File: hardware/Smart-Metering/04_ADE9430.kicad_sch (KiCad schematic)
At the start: 14 parts, among them U401 ADE9430ACPZ, Y401 24.576MHz

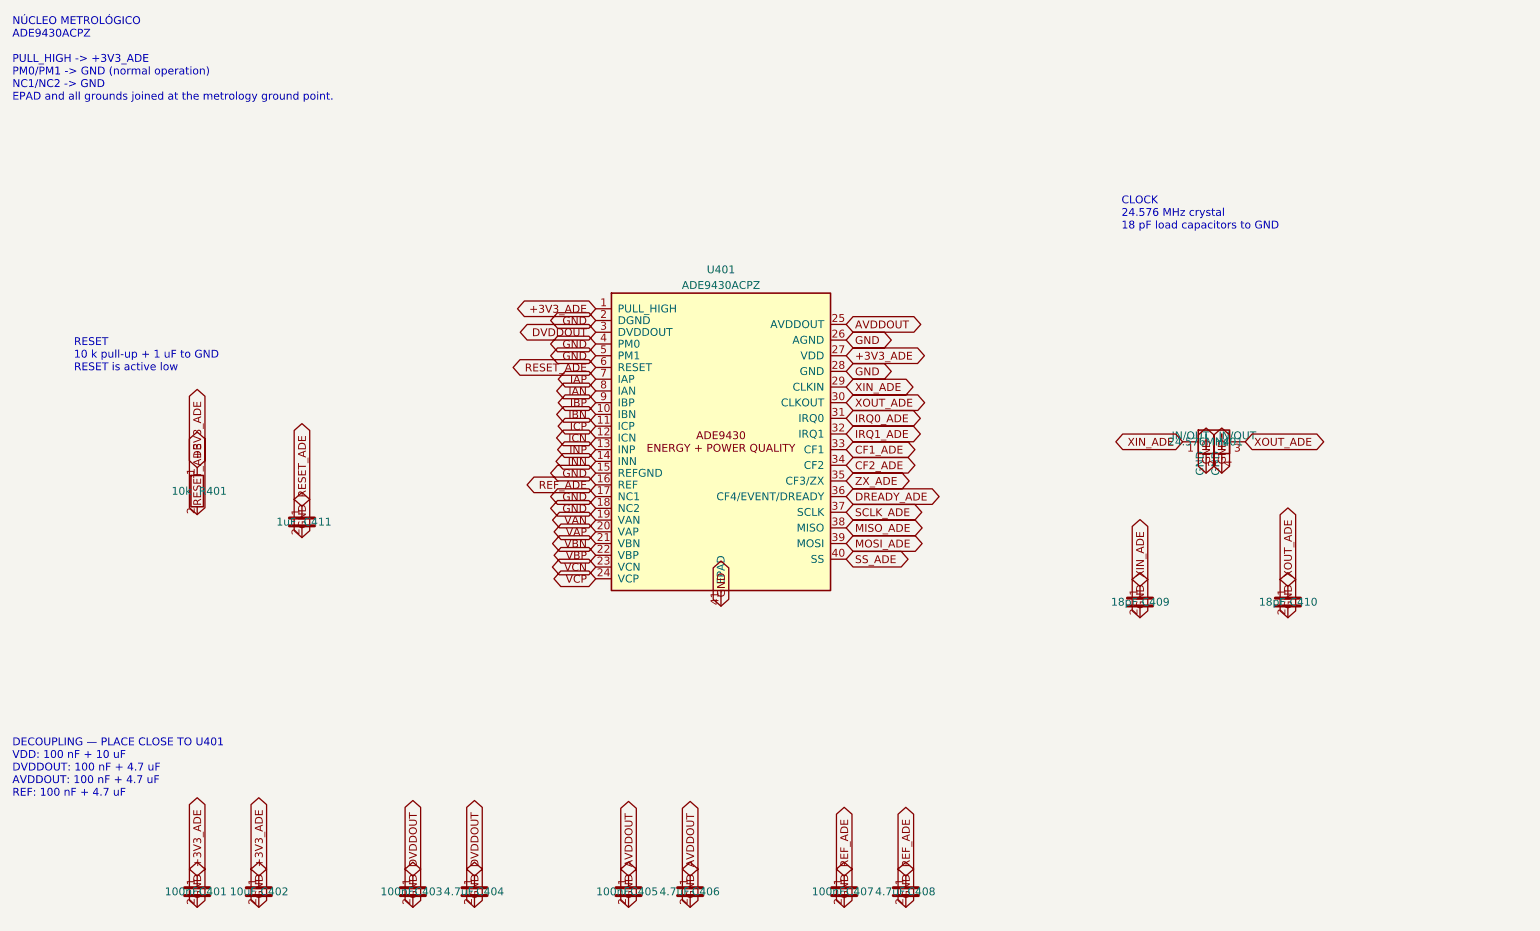
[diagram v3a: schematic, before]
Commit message: Resolve as pendências da revisão do esquemático
P1  ADE9430: footprint VQFN-40 6x6 com EP de 4,15 mm, compatível com as
    variantes CP-40 de 6x6 mm (EP de 3,9 a 4,7 mm).
P2  Confirmado no datasheet: MISO solto com SS alto (pull-up de 100 kΩ)
    e NC1/NC2 em GND, como já estava.
P3  J301-J304: headers JST PH de 4 vias cabeados até conectores M8
    fêmea de painel (à prova de toque).
P4  PS601 -> U606 ADuM6000 (isoPower 5 kVrms, símbolo oficial).
P5  PS101 -> RAC20-05SK/277 (85-305 VAC, 120-430 VDC, 20 W); fusíveis
    T500mA, R101 3 W, C101 10 uF/450 V; entrada do BQ25895 a 3 A.
P7  TPS61089 -> TPS61022 (compensação interna, sem valores a ajustar).
P8  Placa EV alimentada pelos pinos 5 V do J1 (nota na folha 07).
P9  EEPROM de calibração 24LC64 no I2C1.
P10 Labels globais de uma só folha convertidos em locais.

Verificação: 223 componentes, nenhum pino solto, nenhuma net sem fonte,
nenhum conflito de saída, isolação íntegra, todos os footprints
existentes na biblioteca oficial do KiCad.

Co-Authored-By: Claude Opus 5.5 <noreply@anthropic.com>
Claude-Session: https://claude.ai/code/session_012B8cVkhtjf3eg98UdpNCpf
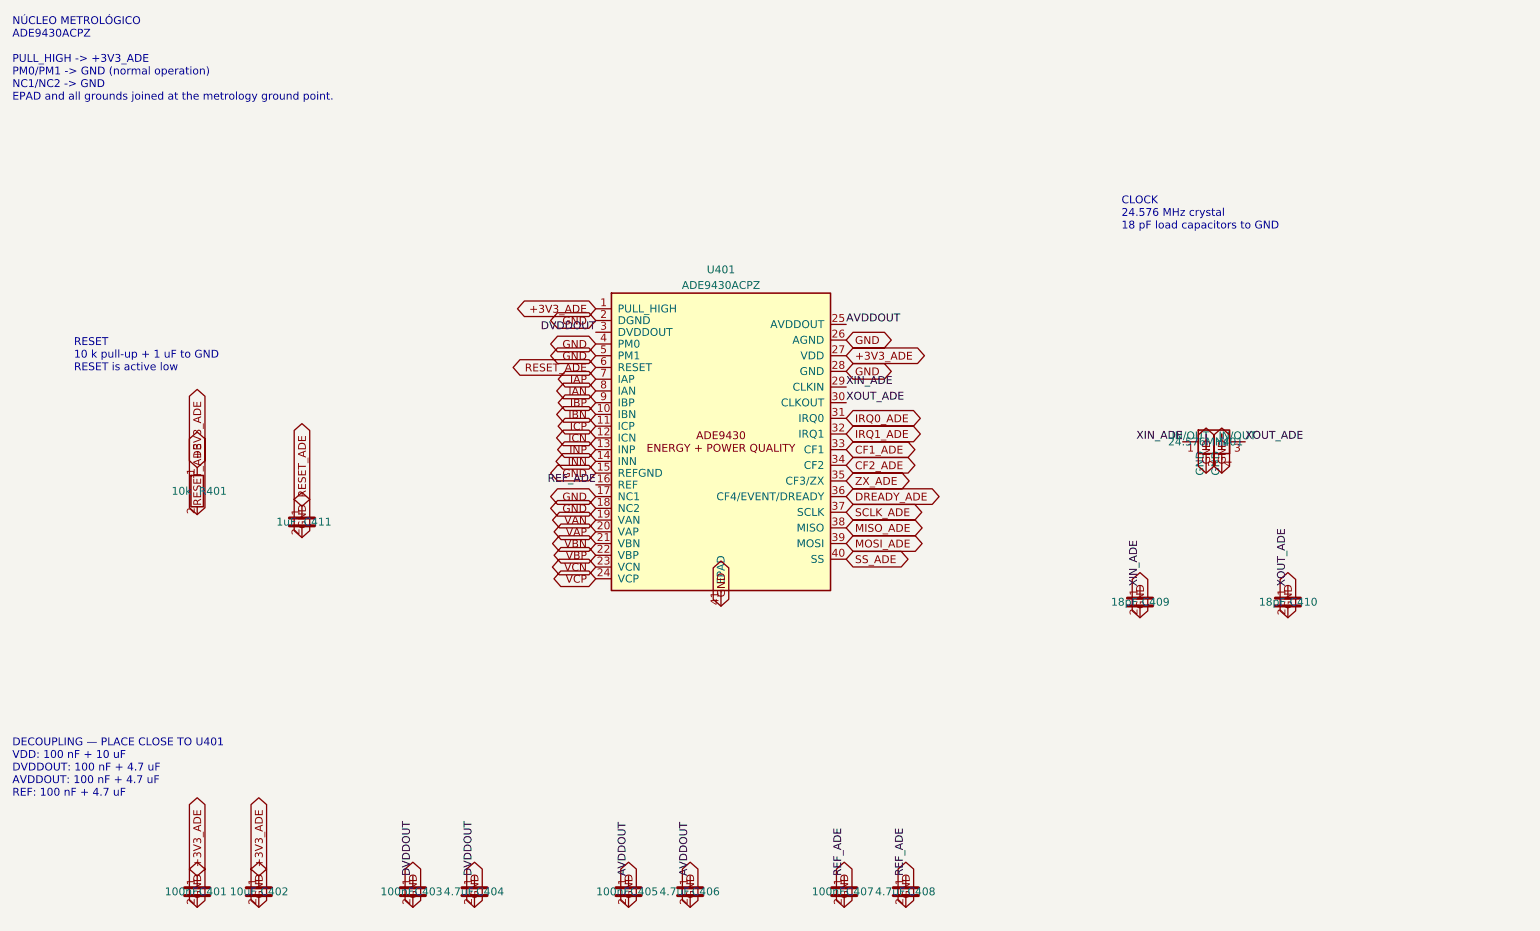
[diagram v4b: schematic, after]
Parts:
- U401: footprint Package_DFN_QFN:QFN-40-1EP_6x6mm_P0.5mm_EP4.6x4.6mm -> Package_DFN_QFN:Texas_RHA0040B_VQFN-40-1EP_6x6mm_P0.5mm_EP4.15x4.15mm
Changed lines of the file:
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@@
 		(property "Intersheetrefs" "${INTERSHEET_REFS}" (at 119.68 72.315 0) (hide yes) (effects (font (size 1.27 1.27))))
 	)
-	(global_label "DVDDOUT" (shape bidirectional) (at 119.68 74.22 180)
-		(effects (font (size 1.27 1.27)) (justify right))
-		(property "Intersheetrefs" "${INTERSHEET_REFS}" (at 119.68 74.22 0) (hide yes) (effects (font (size 1.27 1.27))))
+	(label "DVDDOUT" (at 119.68 74.22 180)
+		(effects (font (size 1.27 1.27)) (justify right bottom))
 	)
 	(global_label "GND" (shape bidirectional) (at 119.68 76.125 180)
@@
 		(property "Intersheetrefs" "${INTERSHEET_REFS}" (at 119.68 97.08 0) (hide yes) (effects (font (size 1.27 1.27))))
 	)
-	(global_label "REF_ADE" (shape bidirectional) (at 119.68 98.985 180)
-		(effects (font (size 1.27 1.27)) (justify right))
-		(property "Intersheetrefs" "${INTERSHEET_REFS}" (at 119.68 98.985 0) (hide yes) (effects (font (size 1.27 1.27))))
+	(label "REF_ADE" (at 119.68 98.985 180)
+		(effects (font (size 1.27 1.27)) (justify right bottom))
 	)
 	(global_label "GND" (shape bidirectional) (at 119.68 100.89 180)
@@
 		(property "Intersheetrefs" "${INTERSHEET_REFS}" (at 119.68 114.225 0) (hide yes) (effects (font (size 1.27 1.27))))
 	)
-	(global_label "AVDDOUT" (shape bidirectional) (at 160.32 72.95 0)
-		(effects (font (size 1.27 1.27)) (justify left))
-		(property "Intersheetrefs" "${INTERSHEET_REFS}" (at 160.32 72.95 0) (hide yes) (effects (font (size 1.27 1.27))))
+	(label "AVDDOUT" (at 160.32 72.95 0)
+		(effects (font (size 1.27 1.27)) (justify left bottom))
 	)
 	(global_label "GND" (shape bidirectional) (at 160.32 75.49 0)
@@
 		(property "Intersheetrefs" "${INTERSHEET_REFS}" (at 160.32 80.57 0) (hide yes) (effects (font (size 1.27 1.27))))
 	)
-	(global_label "XIN_ADE" (shape bidirectional) (at 160.32 83.11 0)
-		(effects (font (size 1.27 1.27)) (justify left))
-		(property "Intersheetrefs" "${INTERSHEET_REFS}" (at 160.32 83.11 0) (hide yes) (effects (font (size 1.27 1.27))))
-	)
-	(global_label "XOUT_ADE" (shape bidirectional) (at 160.32 85.64999999999999 0)
-		(effects (font (size 1.27 1.27)) (justify left))
-		(property "Intersheetrefs" "${INTERSHEET_REFS}" (at 160.32 85.64999999999999 0) (hide yes) (effects (font (size 1.27 1.27))))
+	(label "XIN_ADE" (at 160.32 83.11 0)
+		(effects (font (size 1.27 1.27)) (justify left bottom))
+	)
+	(label "XOUT_ADE" (at 160.32 85.64999999999999 0)
+		(effects (font (size 1.27 1.27)) (justify left bottom))
 	)
 	(global_label "IRQ0_ADE" (shape bidirectional) (at 160.32 88.19 0)
@@
 		(property "Reference" "U401" (at 140 64.06 0) (effects (font (size 1.27 1.27))))
 		(property "Value" "ADE9430ACPZ" (at 140 66.6 0) (effects (font (size 1.27 1.27))))
-		(property "Footprint" "Package_DFN_QFN:QFN-40-1EP_6x6mm_P0.5mm_EP4.6x4.6mm" (at 140 92 0) (effects (font (size 1.27 1.27)) (hide yes)))
+		(property "Footprint" "Package_DFN_QFN:Texas_RHA0040B_VQFN-40-1EP_6x6mm_P0.5mm_EP4.15x4.15mm" (at 140 92 0) (effects (font (size 1.27 1.27)) (hide yes)))
 		(property "Datasheet" "https://www.analog.com/media/en/technical-documentation/data-sheets/ade9430.pdf" (at 140 92 0) (effects (font (size 1.27 1.27)) (hide yes)))
 		(property "Description" "High performance polyphase energy and Class S power quality monitoring IC" (at 140 92 0) (effects (font (size 1.27 1.27)) (hide yes)))
@@
 		)
 	)
-	(global_label "DVDDOUT" (shape bidirectional) (at 90 162.46 90)
-		(effects (font (size 1.27 1.27)) (justify left))
-		(property "Intersheetrefs" "${INTERSHEET_REFS}" (at 90 162.46 0) (hide yes) (effects (font (size 1.27 1.27))))
+	(label "DVDDOUT" (at 90 162.46 90)
+		(effects (font (size 1.27 1.27)) (justify left bottom))
 	)
 	(global_label "GND" (shape bidirectional) (at 90 167.54 270)
@@
 		)
 	)
-	(global_label "DVDDOUT" (shape bidirectional) (at 100 162.46 90)
-		(effects (font (size 1.27 1.27)) (justify left))
-		(property "Intersheetrefs" "${INTERSHEET_REFS}" (at 100 162.46 0) (hide yes) (effects (font (size 1.27 1.27))))
+	(label "DVDDOUT" (at 100 162.46 90)
+		(effects (font (size 1.27 1.27)) (justify left bottom))
 	)
 	(global_label "GND" (shape bidirectional) (at 100 167.54 270)
@@
 		)
 	)
-	(global_label "AVDDOUT" (shape bidirectional) (at 125 162.46 90)
-		(effects (font (size 1.27 1.27)) (justify left))
-		(property "Intersheetrefs" "${INTERSHEET_REFS}" (at 125 162.46 0) (hide yes) (effects (font (size 1.27 1.27))))
+	(label "AVDDOUT" (at 125 162.46 90)
+		(effects (font (size 1.27 1.27)) (justify left bottom))
 	)
 	(global_label "GND" (shape bidirectional) (at 125 167.54 270)
@@
 		)
 	)
-	(global_label "AVDDOUT" (shape bidirectional) (at 135 162.46 90)
-		(effects (font (size 1.27 1.27)) (justify left))
-		(property "Intersheetrefs" "${INTERSHEET_REFS}" (at 135 162.46 0) (hide yes) (effects (font (size 1.27 1.27))))
+	(label "AVDDOUT" (at 135 162.46 90)
+		(effects (font (size 1.27 1.27)) (justify left bottom))
 	)
 	(global_label "GND" (shape bidirectional) (at 135 167.54 270)
@@
 		)
 	)
-	(global_label "REF_ADE" (shape bidirectional) (at 160 162.46 90)
-		(effects (font (size 1.27 1.27)) (justify left))
-		(property "Intersheetrefs" "${INTERSHEET_REFS}" (at 160 162.46 0) (hide yes) (effects (font (size 1.27 1.27))))
+	(label "REF_ADE" (at 160 162.46 90)
+		(effects (font (size 1.27 1.27)) (justify left bottom))
 	)
 	(global_label "GND" (shape bidirectional) (at 160 167.54 270)
@@
 		)
 	)
-	(global_label "REF_ADE" (shape bidirectional) (at 170 162.46 90)
-		(effects (font (size 1.27 1.27)) (justify left))
-		(property "Intersheetrefs" "${INTERSHEET_REFS}" (at 170 162.46 0) (hide yes) (effects (font (size 1.27 1.27))))
+	(label "REF_ADE" (at 170 162.46 90)
+		(effects (font (size 1.27 1.27)) (justify left bottom))
 	)
 	(global_label "GND" (shape bidirectional) (at 170 167.54 270)
@@
 		)
 	)
-	(global_label "XIN_ADE" (shape bidirectional) (at 214.92 92 180)
-		(effects (font (size 1.27 1.27)) (justify right))
-		(property "Intersheetrefs" "${INTERSHEET_REFS}" (at 214.92 92 0) (hide yes) (effects (font (size 1.27 1.27))))
-	)
-	(global_label "XOUT_ADE" (shape bidirectional) (at 225.08 92 0)
-		(effects (font (size 1.27 1.27)) (justify left))
-		(property "Intersheetrefs" "${INTERSHEET_REFS}" (at 225.08 92 0) (hide yes) (effects (font (size 1.27 1.27))))
+	(label "XIN_ADE" (at 214.92 92 180)
+		(effects (font (size 1.27 1.27)) (justify right bottom))
+	)
+	(label "XOUT_ADE" (at 225.08 92 0)
+		(effects (font (size 1.27 1.27)) (justify left bottom))
 	)
 	(global_label "GND" (shape bidirectional) (at 218.73 97.08 270)
@@
 		)
 	)
-	(global_label "XIN_ADE" (shape bidirectional) (at 208 115.46 90)
-		(effects (font (size 1.27 1.27)) (justify left))
-		(property "Intersheetrefs" "${INTERSHEET_REFS}" (at 208 115.46 0) (hide yes) (effects (font (size 1.27 1.27))))
+	(label "XIN_ADE" (at 208 115.46 90)
+		(effects (font (size 1.27 1.27)) (justify left bottom))
 	)
 	(global_label "GND" (shape bidirectional) (at 208 120.54 270)
@@
 		)
 	)
-	(global_label "XOUT_ADE" (shape bidirectional) (at 232 115.46 90)
-		(effects (font (size 1.27 1.27)) (justify left))
-		(property "Intersheetrefs" "${INTERSHEET_REFS}" (at 232 115.46 0) (hide yes) (effects (font (size 1.27 1.27))))
+	(label "XOUT_ADE" (at 232 115.46 90)
+		(effects (font (size 1.27 1.27)) (justify left bottom))
 	)
 	(global_label "GND" (shape bidirectional) (at 232 120.54 270)

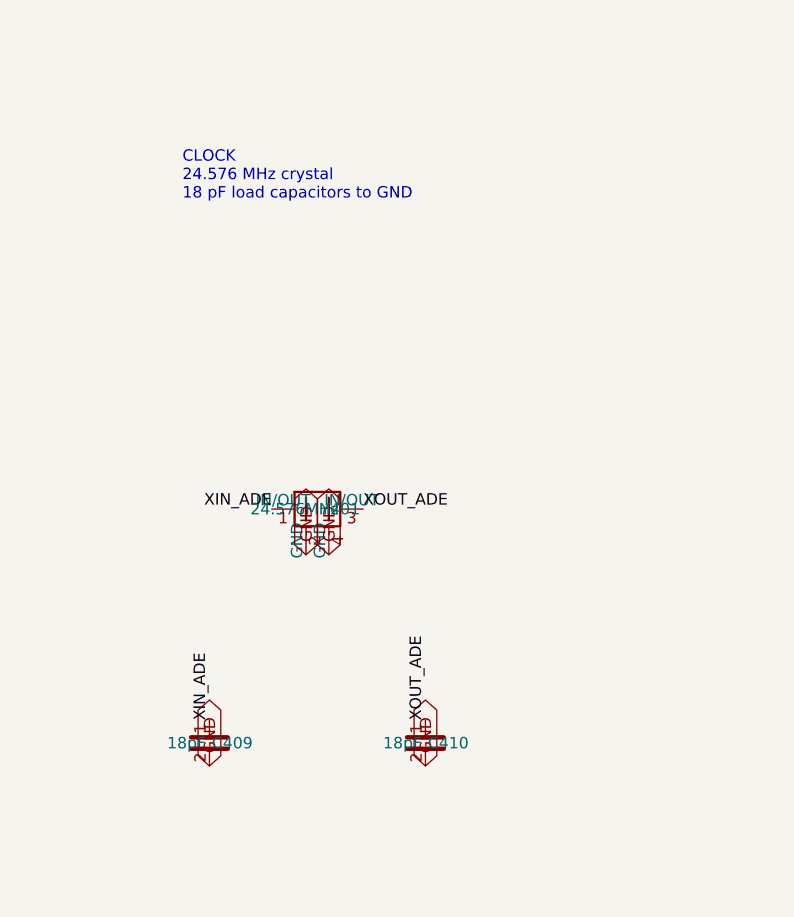
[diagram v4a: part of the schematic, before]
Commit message: Integra a mecânica (modelo 3D) e os documentos do branch minhas-alteracoes (#3)
* Integra a mecânica e os documentos do branch minhas-alteracoes na main

- pasta 'modelo 3D/' (Onshape e Fusion: montagens, STEP, scripts); os
  FeatureScripts de cad/ passam para 'modelo 3D/Onshape/' sem alteração;
- AGENTS.md e docs DECISIONS, INTERNAL_BATTERY, POWER_CLOCK,
  VOLTAGE_SENSING, WORKFLOW, REVIEW_2026-10-02 e UPS_AUTONOMY, atualizados
  para o esquemático e o layout da main (divisor 5x200k+1k, ADuM6000 +
  TPS7A2033, BQ25895 + J901, RAC20); a versão anterior fica como histórico;
- decisão D-005 aplicada: Y401 ABM8-24.576MHZ-8-D1X-T (CL 8 pF) e
  C409/C410 de 10 pF C0G (antes 18 pF), no esquemático e na placa;
- novas decisões D-007 a D-011 e REQ-011 (alimentação e bateria interna);
  pendência P1: ~CE do BQ25895 em GND (carga habilitada antes do firmware).

A folha 10_Battery_Interface do branch não entra: a interface da bateria
já é o J901 da folha 09.

Co-Authored-By: Claude Opus 5.5 <noreply@anthropic.com>
Claude-Session: https://claude.ai/code/session_012B8cVkhtjf3eg98UdpNCpf

* Corrige os scripts do Fusion apontados na revisão do PR #3

- Exporta todos os STEP antes de ocultar carcaça e painel (os dois saíam vazios).
- Pasta do Fusion derivada da posição do script, sem caminho F:\ fixo.
- Posições e rotações lidas de mounting.json.
- Relatório e mensagem informam pares de interferência não verificados.
- Registra os STEP vazios da exportação atual e corrige espaços em UPS_AUTONOMY.

Co-Authored-By: Claude Opus 5.5 <noreply@anthropic.com>
Claude-Session: https://claude.ai/code/session_012B8cVkhtjf3eg98UdpNCpf

---------

Co-authored-by: Claude <noreply@anthropic.com>
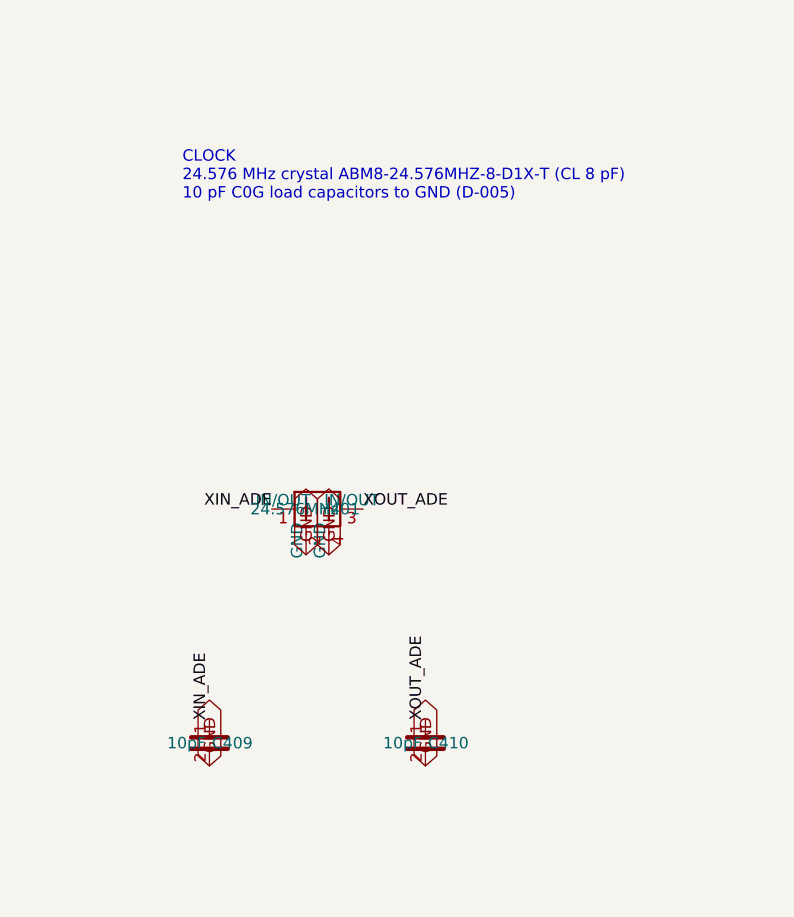
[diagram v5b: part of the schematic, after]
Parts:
- C409, C410: value 18pF -> 10pF
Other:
- note added: "CLOCK 24.576 MHz crystal ABM8-24.576MHZ-8-D1X-T (CL 8 pF) 10 pF C0G load capacitors to GND (D-005)"
- note removed: "CLOCK 24.576 MHz crystal 18 pF load capacitors to GND"
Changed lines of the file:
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@@
 		(effects (font (size 1.27 1.27)) (justify left))
 	)
-	(text "CLOCK\n24.576 MHz crystal\n18 pF load capacitors to GND"
+	(text "CLOCK\n24.576 MHz crystal ABM8-24.576MHZ-8-D1X-T (CL 8 pF)\n10 pF C0G load capacitors to GND (D-005)"
 		(exclude_from_sim no)(at 205 55 0)
 		(effects (font (size 1.27 1.27)) (justify left))
@@
 		(property "Footprint" "Crystal:Crystal_SMD_3225-4Pin_3.2x2.5mm" (at 220 92 0) (effects (font (size 1.27 1.27)) (hide yes)))
 		(property "Datasheet" "" (at 220 92 0) (effects (font (size 1.27 1.27)) (hide yes)))
-		(property "Description" "ADE9430 master crystal, 24.576 MHz" (at 220 92 0) (effects (font (size 1.27 1.27)) (hide yes)))
+		(property "Description" "ADE9430 master crystal, 24.576 MHz, Abracon ABM8-24.576MHZ-8-D1X-T, CL 8 pF" (at 220 92 0) (effects (font (size 1.27 1.27)) (hide yes)))
 		(pin "1")
 		(pin "2")
@@
 		(exclude_from_sim no)(in_bom yes)(on_board yes)(in_pos_files yes)(dnp no)
 		(property "Reference" "C409" (at 210.54 118 0) (effects (font (size 1.27 1.27))))
-		(property "Value" "18pF" (at 205.46 118 0) (effects (font (size 1.27 1.27))))
+		(property "Value" "10pF" (at 205.46 118 0) (effects (font (size 1.27 1.27))))
 		(property "Footprint" "Capacitor_SMD:C_0603_1608Metric" (at 208 118 0) (effects (font (size 1.27 1.27)) (hide yes)))
 		(property "Datasheet" "" (at 208 118 0) (effects (font (size 1.27 1.27)) (hide yes)))
-		(property "Description" "Crystal load capacitor" (at 208 118 0) (effects (font (size 1.27 1.27)) (hide yes)))
+		(property "Description" "Crystal load capacitor, 10 pF C0G 1%" (at 208 118 0) (effects (font (size 1.27 1.27)) (hide yes)))
 		(pin "1")
 		(pin "2")
@@
 		(exclude_from_sim no)(in_bom yes)(on_board yes)(in_pos_files yes)(dnp no)
 		(property "Reference" "C410" (at 234.54 118 0) (effects (font (size 1.27 1.27))))
-		(property "Value" "18pF" (at 229.46 118 0) (effects (font (size 1.27 1.27))))
+		(property "Value" "10pF" (at 229.46 118 0) (effects (font (size 1.27 1.27))))
 		(property "Footprint" "Capacitor_SMD:C_0603_1608Metric" (at 232 118 0) (effects (font (size 1.27 1.27)) (hide yes)))
 		(property "Datasheet" "" (at 232 118 0) (effects (font (size 1.27 1.27)) (hide yes)))
-		(property "Description" "Crystal load capacitor" (at 232 118 0) (effects (font (size 1.27 1.27)) (hide yes)))
-		(pin "1")
-		(pin "2")
+		(property "Description" "Crystal load capacitor, 10 pF C0G 1%" (at 232 118 0) (effects (font (size 1.27 1.27)) (hide yes)))
+		(pin "1")
+		(pin "2")
